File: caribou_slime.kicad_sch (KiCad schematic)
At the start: 12 parts, among them SW1 SW_DIP_x01, U1 ESP32-C3_SUPERMINI, U2 BMI270

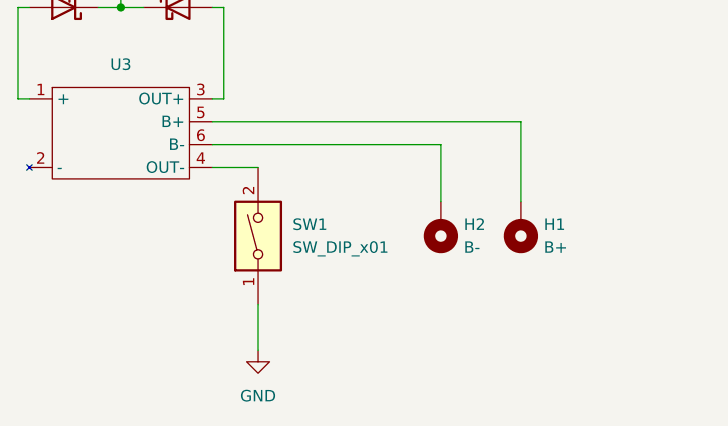
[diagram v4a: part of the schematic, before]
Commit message: Change generic switch for EG1270
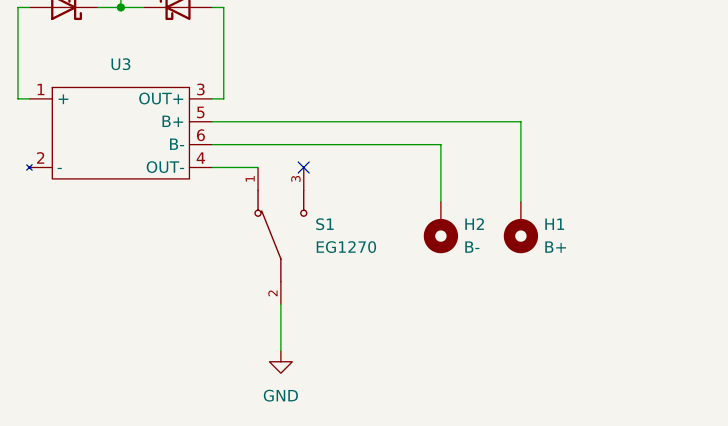
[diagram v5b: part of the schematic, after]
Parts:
- removed SW1: SW_DIP_x01, symbol Switch:SW_DIP_x01
- added S1: EG1270, EG1270:SW_EG1270, symbol EG1270:EG1270
- C1, C2: footprint (none) -> Capacitor_SMD:C_0402_1005Metric_Pad0.74x0.62mm_HandSolder
- H1, H2: footprint (none) -> Connector_PinHeader_2.54mm:PinHeader_1x01_P2.54mm_Horizontal
- R1, R2: footprint (none) -> Resistor_SMD:R_0402_1005Metric_Pad0.72x0.64mm_HandSolder
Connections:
- net GND: now also S1.2
- net at U3.4 (OUT-): now also S1.1
- no-connect marks 18 -> 19
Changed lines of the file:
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@@
   (no_connect (at 81.28 63.5))
   (no_connect (at 45.72 53.34))
+  (no_connect (at 60.96 140.97))
   (no_connect (at 226.06 71.12))
   (no_connect (at 195.58 63.5))
@@
     (stroke (width 0) (type default))
   )
-  (wire (pts (xy 55.88 156.21) (xy 55.88 161.29))
+  (wire (pts (xy 58.42 156.21) (xy 58.42 161.29))
     (stroke (width 0) (type default))
   )
@@
     )
   )
-  (symbol (lib_id "power:GND") (at 55.88 161.29 0) (unit 1)
-    (in_bom yes) (on_board yes) (dnp no) (fields_autoplaced)
-    (property "Reference" "#PWR09" (at 55.88 167.64 0)
-      (effects (font (size 1.27 1.27)) hide)
-    )
-    (property "Value" "GND" (at 55.88 166.37 0)
-      (effects (font (size 1.27 1.27)))
-    )
-    (property "Footprint" "" (at 55.88 161.29 0)
-      (effects (font (size 1.27 1.27)) hide)
-    )
-    (property "Datasheet" "" (at 55.88 161.29 0)
+  (symbol (lib_id "power:GND") (at 58.42 161.29 0) (unit 1)
+    (in_bom yes) (on_board yes) (dnp no) (fields_autoplaced)
+    (property "Reference" "#PWR09" (at 58.42 167.64 0)
+      (effects (font (size 1.27 1.27)) hide)
+    )
+    (property "Value" "GND" (at 58.42 166.37 0)
+      (effects (font (size 1.27 1.27)))
+    )
+    (property "Footprint" "" (at 58.42 161.29 0)
+      (effects (font (size 1.27 1.27)) hide)
+    )
+    (property "Datasheet" "" (at 58.42 161.29 0)
       (effects (font (size 1.27 1.27)) hide)
     )
@@
       (effects (font (size 1.27 1.27)) (justify left))
     )
-    (property "Footprint" "" (at 176.022 50.8 90)
+    (property "Footprint" "Resistor_SMD:R_0402_1005Metric_Pad0.72x0.64mm_HandSolder" (at 176.022 50.8 90)
       (effects (font (size 1.27 1.27)) hide)
     )
@@
       (effects (font (size 1.27 1.27)) (justify right))
     )
-    (property "Footprint" "" (at 85.09 147.32 0)
+    (property "Footprint" "Connector_PinHeader_2.54mm:PinHeader_1x01_P2.54mm_Horizontal" (at 85.09 147.32 0)
       (effects (font (size 1.27 1.27)) hide)
     )
@@
     )
   )
-  (symbol (lib_id "Switch:SW_DIP_x01") (at 55.88 148.59 90) (unit 1)
-    (in_bom yes) (on_board yes) (dnp no)
-    (property "Reference" "SW1" (at 59.69 147.32 90)
+  (symbol (lib_id "EG1270:EG1270") (at 58.42 148.59 90) (unit 1)
+    (in_bom yes) (on_board yes) (dnp no) (fields_autoplaced)
+    (property "Reference" "S1" (at 62.23 147.32 90)
       (effects (font (size 1.27 1.27)) (justify right))
     )
-    (property "Value" "SW_DIP_x01" (at 59.69 149.86 90)
+    (property "Value" "EG1270" (at 62.23 149.86 90)
       (effects (font (size 1.27 1.27)) (justify right))
     )
-    (property "Footprint" "" (at 55.88 148.59 0)
-      (effects (font (size 1.27 1.27)) hide)
-    )
-    (property "Datasheet" "~" (at 55.88 148.59 0)
-      (effects (font (size 1.27 1.27)) hide)
-    )
-    (pin "1")
-    (pin "2")
-    (instances
-      (project "caribou_slime"
-        (path "/61bfc64c-87c3-434a-8ade-1f9e7b05e459"
-          (reference "SW1") (unit 1)
+    (property "Footprint" "EG1270:SW_EG1270" (at 58.42 148.59 0)
+      (effects (font (size 1.27 1.27)) (justify bottom) hide)
+    )
+    (property "Datasheet" "" (at 58.42 148.59 0)
+      (effects (font (size 1.27 1.27)) hide)
+    )
+    (property "MF" "E-Switch" (at 58.42 148.59 0)
+      (effects (font (size 1.27 1.27)) (justify bottom) hide)
+    )
+    (property "MAXIMUM_PACKAGE_HEIGHT" "4.0 mm" (at 58.42 148.59 0)
+      (effects (font (size 1.27 1.27)) (justify bottom) hide)
+    )
+    (property "Package" "None" (at 58.42 148.59 0)
+      (effects (font (size 1.27 1.27)) (justify bottom) hide)
+    )
+    (property "Price" "None" (at 58.42 148.59 0)
+      (effects (font (size 1.27 1.27)) (justify bottom) hide)
+    )
+    (property "Check_prices" "https://www.snapeda.com/parts/EG1270/E-Switch/view-part/?ref=eda" (at 58.42 148.59 0)
+      (effects (font (size 1.27 1.27)) (justify bottom) hide)
+    )
+    (property "STANDARD" "Manufacturer Recommendations" (at 58.42 148.59 0)
+      (effects (font (size 1.27 1.27)) (justify bottom) hide)
+    )
+    (property "PARTREV" "-" (at 58.42 148.59 0)
+      (effects (font (size 1.27 1.27)) (justify bottom) hide)
+    )
+    (property "SnapEDA_Link" "https://www.snapeda.com/parts/EG1270/E-Switch/view-part/?ref=snap" (at 58.42 148.59 0)
+      (effects (font (size 1.27 1.27)) (justify bottom) hide)
+    )
+    (property "MP" "EG1270" (at 58.42 148.59 0)
+      (effects (font (size 1.27 1.27)) (justify bottom) hide)
+    )
+    (property "Purchase-URL" "https://www.snapeda.com/api/url_track_click_mouser/?unipart_id=186937&manufacturer=E-Switch&part_name=EG1270&search_term=ss22f32" (at 58.42 148.59 0)
+      (effects (font (size 1.27 1.27)) (justify bottom) hide)
+    )
+    (property "Description" "\nSlide Switch, EG Series, SPDT, Non-Shorting, ON-ON, 300mA DC, 6VDC, R/A, PC | E-Switch EG1270\n" (at 58.42 148.59 0)
+      (effects (font (size 1.27 1.27)) (justify bottom) hide)
+    )
+    (property "MANUFACTURER" "E-Switch" (at 58.42 148.59 0)
+      (effects (font (size 1.27 1.27)) (justify bottom) hide)
+    )
+    (property "Availability" "In Stock" (at 58.42 148.59 0)
+      (effects (font (size 1.27 1.27)) (justify bottom) hide)
+    )
+    (property "SNAPEDA_PN" "EG1270" (at 58.42 148.59 0)
+      (effects (font (size 1.27 1.27)) (justify bottom) hide)
+    )
+    (pin "2")
+    (pin "3")
+    (pin "1")
+    (instances
+      (project "caribou_slime"
+        (path "/61bfc64c-87c3-434a-8ade-1f9e7b05e459"
+          (reference "S1") (unit 1)
         )
       )
@@
       (effects (font (size 1.27 1.27)) (justify right))
     )
-    (property "Footprint" "" (at 76.2 147.32 0)
+    (property "Footprint" "Connector_PinHeader_2.54mm:PinHeader_1x01_P2.54mm_Horizontal" (at 76.2 147.32 0)
       (effects (font (size 1.27 1.27)) hide)
     )
@@
       (effects (font (size 1.27 1.27)) (justify left))
     )
-    (property "Footprint" "" (at 246.0752 54.61 0)
+    (property "Footprint" "Capacitor_SMD:C_0402_1005Metric_Pad0.74x0.62mm_HandSolder" (at 246.0752 54.61 0)
       (effects (font (size 1.27 1.27)) hide)
     )
@@
       (effects (font (size 1.27 1.27)) (justify left))
     )
-    (property "Footprint" "" (at 232.1052 54.61 0)
+    (property "Footprint" "Capacitor_SMD:C_0402_1005Metric_Pad0.74x0.62mm_HandSolder" (at 232.1052 54.61 0)
       (effects (font (size 1.27 1.27)) hide)
     )
@@
       (effects (font (size 1.27 1.27)) (justify left))
     )
-    (property "Footprint" "" (at 164.592 50.8 90)
-      (effects (font (size 1.27 1.27)) hide)
-    )
+    (property "Footprint" "Resistor_SMD:R_0402_1005Metric_Pad0.72x0.64mm_HandSolder" (at 164.592 50.8 90)
+      (effects (font (size 1.27 1.27)) hide)
+    )

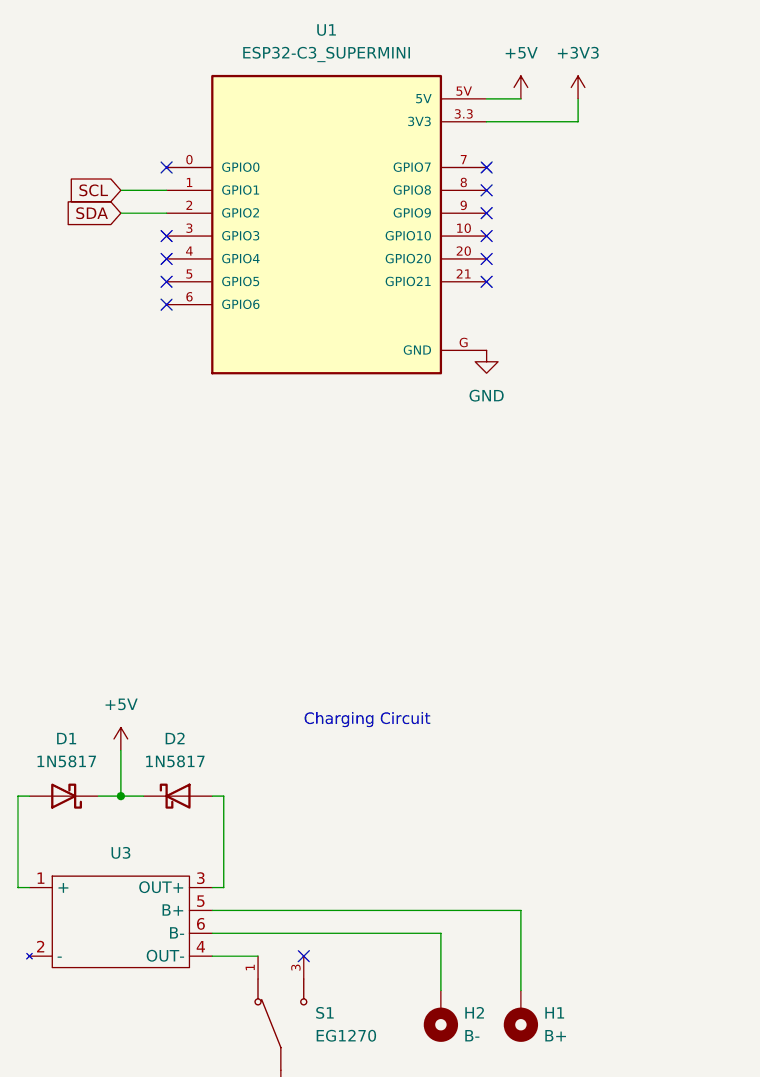
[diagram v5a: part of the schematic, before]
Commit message: Add battery sense, correct I2C connection
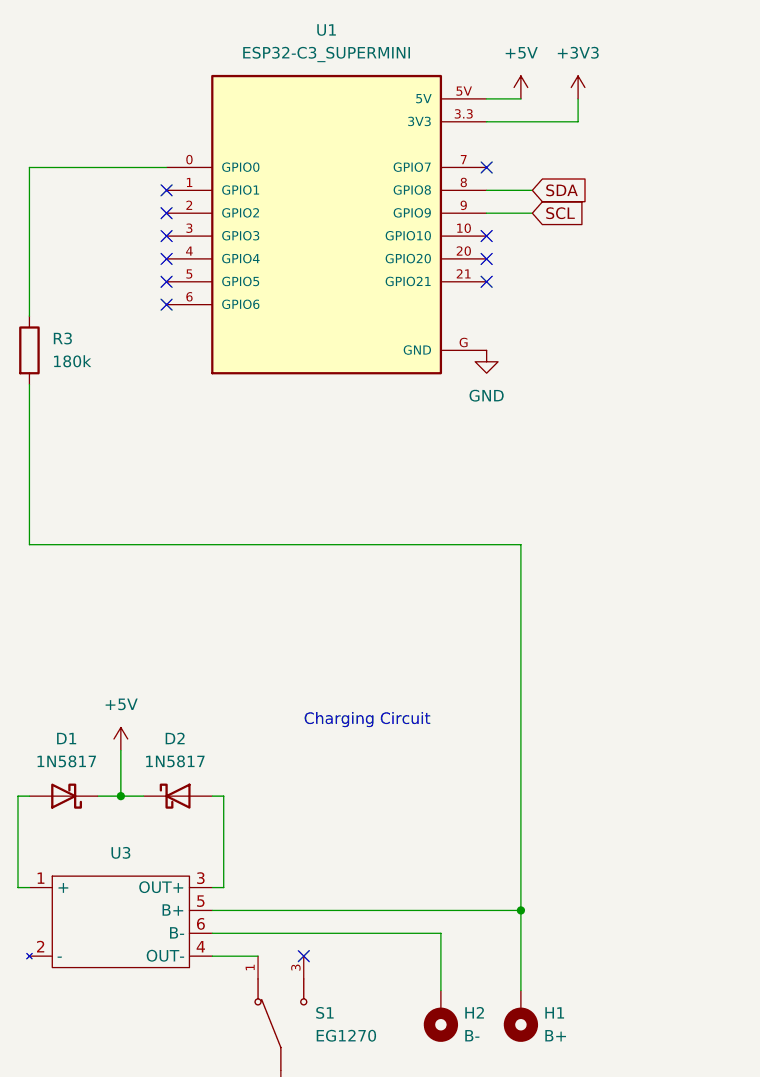
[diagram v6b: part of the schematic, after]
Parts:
- added R3: 180k, Resistor_SMD:R_0402_1005Metric_Pad0.72x0.64mm_HandSolder, symbol Device:R
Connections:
- net SCL: now also U1.9 (GPIO9); no longer U1.1 (GPIO1)
- net SDA: now also U1.8 (GPIO8); no longer U1.2 (GPIO2)
- net at H1.1, U3.5 (B+): now also R3.2
- net at U1.0 (GPIO0): now also R3.1
- no-connect marks 19 -> 18
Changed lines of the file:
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@@
   (junction (at 226.06 77.47) (diameter 0) (color 0 0 0 0)
+  )
+  (junction (at 85.09 135.89) (diameter 0) (color 0 0 0 0)
   )
   (junction (at 177.8 58.42) (diameter 0) (color 0 0 0 0)
@@
   (no_connect (at 195.58 68.58))
   (no_connect (at 226.06 50.8))
-  (no_connect (at 81.28 55.88))
+  (no_connect (at 45.72 55.88))
   (no_connect (at 45.72 66.04))
   (no_connect (at 81.28 60.96))
   (no_connect (at 81.28 63.5))
-  (no_connect (at 45.72 53.34))
   (no_connect (at 60.96 140.97))
   (no_connect (at 226.06 71.12))
@@
   (no_connect (at 81.28 66.04))
   (no_connect (at 45.72 60.96))
-  (no_connect (at 81.28 58.42))
+  (no_connect (at 45.72 58.42))
   (no_connect (at 81.28 53.34))
   (no_connect (at 45.72 68.58))
@@
     (stroke (width 0) (type default))
   )
-  (wire (pts (xy 40.64 58.42) (xy 45.72 58.42))
+  (wire (pts (xy 30.48 53.34) (xy 45.72 53.34))
     (stroke (width 0) (type default))
   )
@@
     (stroke (width 0) (type default))
   )
+  (wire (pts (xy 81.28 58.42) (xy 86.36 58.42))
+    (stroke (width 0) (type default))
+  )
   (wire (pts (xy 226.06 45.72) (xy 231.14 45.72))
     (stroke (width 0) (type default))
@@
     (stroke (width 0) (type default))
   )
-  (wire (pts (xy 40.64 55.88) (xy 45.72 55.88))
-    (stroke (width 0) (type default))
-  )
   (wire (pts (xy 50.8 133.35) (xy 52.07 133.35))
     (stroke (width 0) (type default))
@@
     (stroke (width 0) (type default))
   )
+  (wire (pts (xy 30.48 95.25) (xy 85.09 95.25))
+    (stroke (width 0) (type default))
+  )
+  (wire (pts (xy 81.28 55.88) (xy 86.36 55.88))
+    (stroke (width 0) (type default))
+  )
   (wire (pts (xy 231.14 45.72) (xy 231.14 46.99))
     (stroke (width 0) (type default))
@@
     (stroke (width 0) (type default))
   )
+  (wire (pts (xy 30.48 69.85) (xy 30.48 53.34))
+    (stroke (width 0) (type default))
+  )
   (wire (pts (xy 29.21 133.35) (xy 29.21 123.19))
     (stroke (width 0) (type default))
@@
     (stroke (width 0) (type default))
   )
+  (wire (pts (xy 30.48 77.47) (xy 30.48 95.25))
+    (stroke (width 0) (type default))
+  )
   (wire (pts (xy 231.14 43.18) (xy 238.76 43.18))
     (stroke (width 0) (type default))
@@
   )
   (wire (pts (xy 231.14 43.18) (xy 231.14 45.72))
+    (stroke (width 0) (type default))
+  )
+  (wire (pts (xy 85.09 95.25) (xy 85.09 135.89))
     (stroke (width 0) (type default))
   )
@@
     )
   )
-  (global_label "SCL" (shape input) (at 40.64 55.88 180) (fields_autoplaced)
-    (effects (font (size 1.27 1.27)) (justify right))
-    (property "Intersheetrefs" "${INTERSHEET_REFS}" (at 34.1472 55.88 0)
-      (effects (font (size 1.27 1.27)) (justify right) hide)
+  (global_label "SCL" (shape input) (at 86.36 58.42 0) (fields_autoplaced)
+    (effects (font (size 1.27 1.27)) (justify left))
+    (property "Intersheetrefs" "${INTERSHEET_REFS}" (at 92.8528 58.42 0)
+      (effects (font (size 1.27 1.27)) (justify left) hide)
     )
   )
@@
     )
   )
-  (global_label "SDA" (shape input) (at 40.64 58.42 180) (fields_autoplaced)
-    (effects (font (size 1.27 1.27)) (justify right))
-    (property "Intersheetrefs" "${INTERSHEET_REFS}" (at 34.0867 58.42 0)
-      (effects (font (size 1.27 1.27)) (justify right) hide)
+  (global_label "SDA" (shape input) (at 86.36 55.88 0) (fields_autoplaced)
+    (effects (font (size 1.27 1.27)) (justify left))
+    (property "Intersheetrefs" "${INTERSHEET_REFS}" (at 92.9133 55.88 0)
+      (effects (font (size 1.27 1.27)) (justify left) hide)
     )
   )
@@
         )
       )
+    )
+  )
+  (symbol (lib_id "Device:R") (at 30.48 73.66 0) (unit 1)
+    (in_bom yes) (on_board yes) (dnp no) (fields_autoplaced)
+    (property "Reference" "R3" (at 33.02 72.39 0)
+      (effects (font (size 1.27 1.27)) (justify left))
+    )
+    (property "Value" "180k" (at 33.02 74.93 0)
+      (effects (font (size 1.27 1.27)) (justify left))
+    )
+    (property "Footprint" "Resistor_SMD:R_0402_1005Metric_Pad0.72x0.64mm_HandSolder" (at 28.702 73.66 90)
+      (effects (font (size 1.27 1.27)) hide)
+    )
+    (property "Datasheet" "~" (at 30.48 73.66 0)
+      (effects (font (size 1.27 1.27)) hide)
+    )
+    (pin "1")
+    (pin "2")
+    (instances
+      (project "caribou_slime"
+        (path "/61bfc64c-87c3-434a-8ade-1f9e7b05e459"
+          (reference "R3") (unit 1)
+        )
+      )

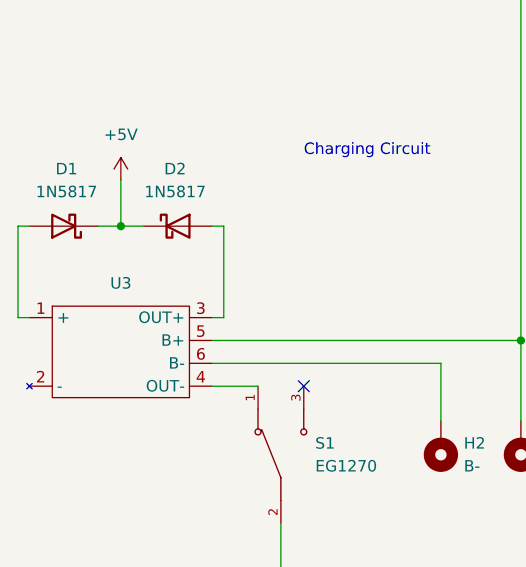
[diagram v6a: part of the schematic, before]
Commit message: Add label on TP4056
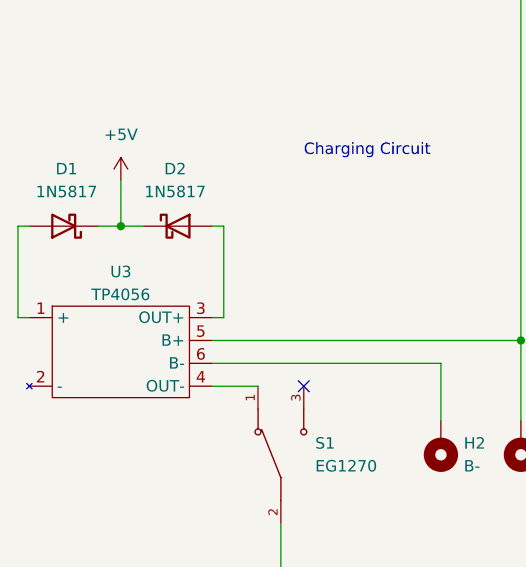
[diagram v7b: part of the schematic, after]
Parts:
- U3: value ~ -> TP4056
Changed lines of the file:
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@@
   )
   (symbol (lib_id "TP4056_Board:TP4056") (at 40.64 143.51 0) (unit 1)
-    (in_bom yes) (on_board yes) (dnp no) (fields_autoplaced)
-    (property "Reference" "U3" (at 40.64 129.54 0)
+    (in_bom yes) (on_board yes) (dnp no)
+    (property "Reference" "U3" (at 40.64 128.27 0)
       (effects (font (size 1.27 1.27)))
     )
-    (property "Value" "~" (at 40.64 143.51 0)
+    (property "Value" "TP4056" (at 40.64 130.81 0)
       (effects (font (size 1.27 1.27)))
     )

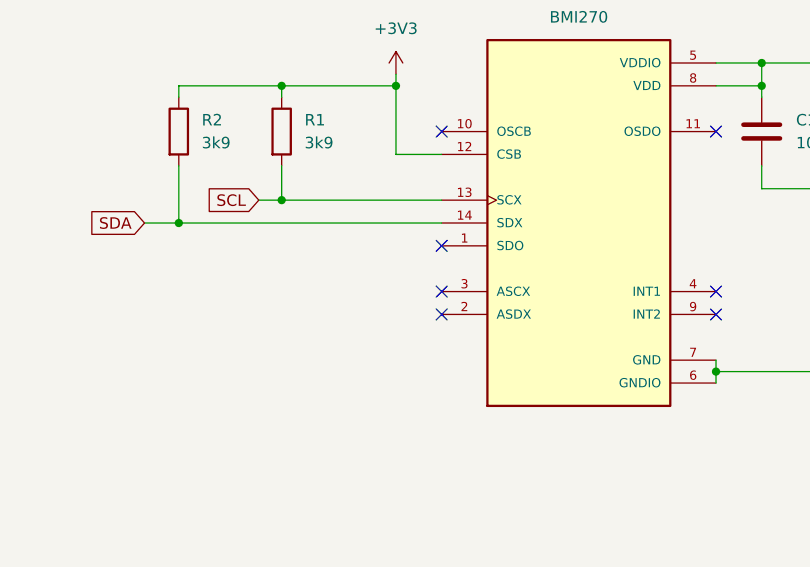
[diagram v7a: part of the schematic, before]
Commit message: Ground SDO on BMI270 to select correct address
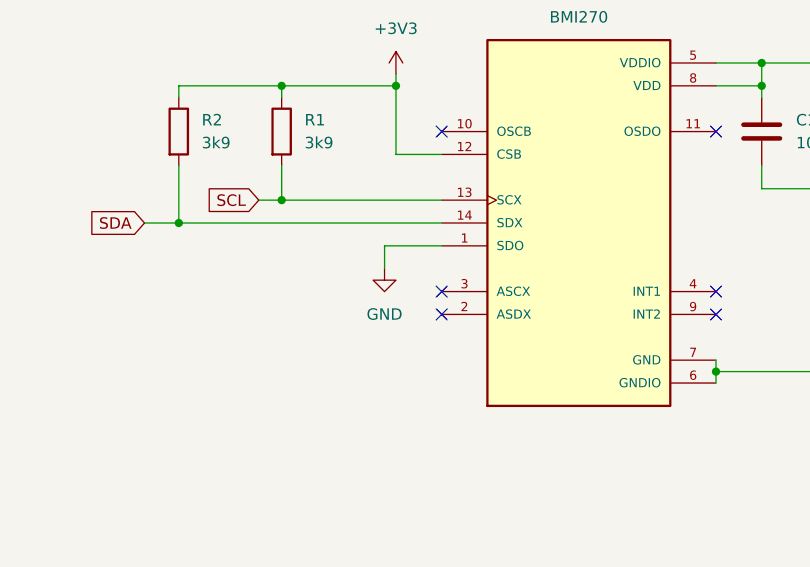
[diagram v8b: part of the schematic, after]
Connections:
- net GND: now also U2.1 (SDO)
- no-connect marks 18 -> 17
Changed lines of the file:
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@@
   (no_connect (at 60.96 140.97))
   (no_connect (at 226.06 71.12))
-  (no_connect (at 195.58 63.5))
   (no_connect (at 45.72 63.5))
   (no_connect (at 195.58 50.8))
@@
     (stroke (width 0) (type default))
   )
+  (wire (pts (xy 189.23 63.5) (xy 195.58 63.5))
+    (stroke (width 0) (type default))
+  )
   (wire (pts (xy 81.28 48.26) (xy 91.44 48.26))
     (stroke (width 0) (type default))
   )
   (wire (pts (xy 91.44 48.26) (xy 91.44 45.72))
+    (stroke (width 0) (type default))
+  )
+  (wire (pts (xy 189.23 66.04) (xy 189.23 63.5))
     (stroke (width 0) (type default))
   )
@@
         )
       )
+    )
+  )
+  (symbol (lib_id "power:GND") (at 189.23 66.04 0) (unit 1)
+    (in_bom yes) (on_board yes) (dnp no) (fields_autoplaced)
+    (property "Reference" "#PWR02" (at 189.23 72.39 0)
+      (effects (font (size 1.27 1.27)) hide)
+    )
+    (property "Value" "GND" (at 189.23 71.12 0)
+      (effects (font (size 1.27 1.27)))
+    )
+    (property "Footprint" "" (at 189.23 66.04 0)
+      (effects (font (size 1.27 1.27)) hide)
+    )
+    (property "Datasheet" "" (at 189.23 66.04 0)
+      (effects (font (size 1.27 1.27)) hide)
+    )
+    (pin "1")
+    (instances
+      (project "caribou_slime"
+        (path "/61bfc64c-87c3-434a-8ade-1f9e7b05e459"
+          (reference "#PWR02") (unit 1)
+        )
+      )
